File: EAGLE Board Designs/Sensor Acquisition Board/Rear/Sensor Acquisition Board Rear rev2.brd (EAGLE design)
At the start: 92.7 x 50.8 mm, 32 parts, among them J1 JUMPER_0603_, J2 CONNECTOR-4_μF_S_RA_, J3 CONNECTOR-4_μF_S_RA_, J4 CONNECTOR-4_μF_S_RA_, J5 CONNECTOR-4_μF_S_RA_, J6 CONNECTOR-CAN_μF_S_RA_, U1 VOLTAGE_REGULATOR_SOT-223_5V, U2 MCP2562FD

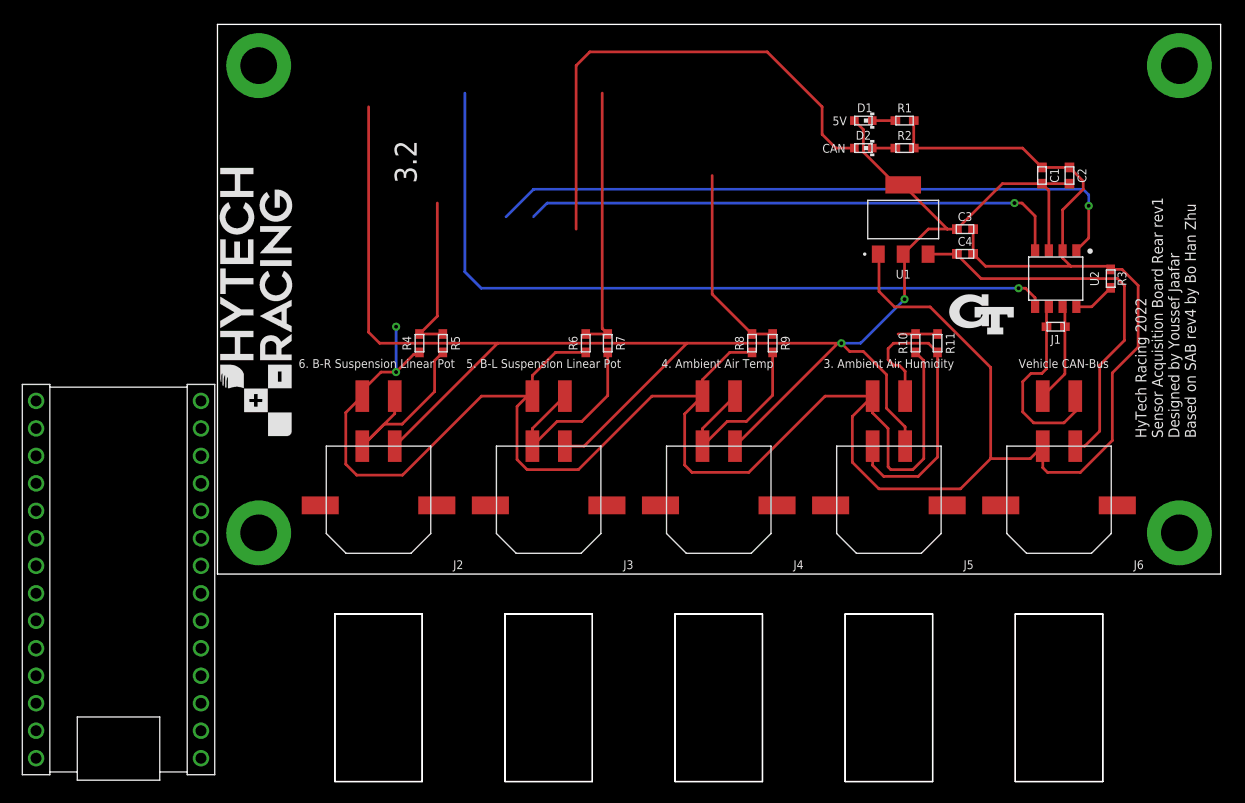
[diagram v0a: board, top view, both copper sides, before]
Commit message: regrounded with groundplane
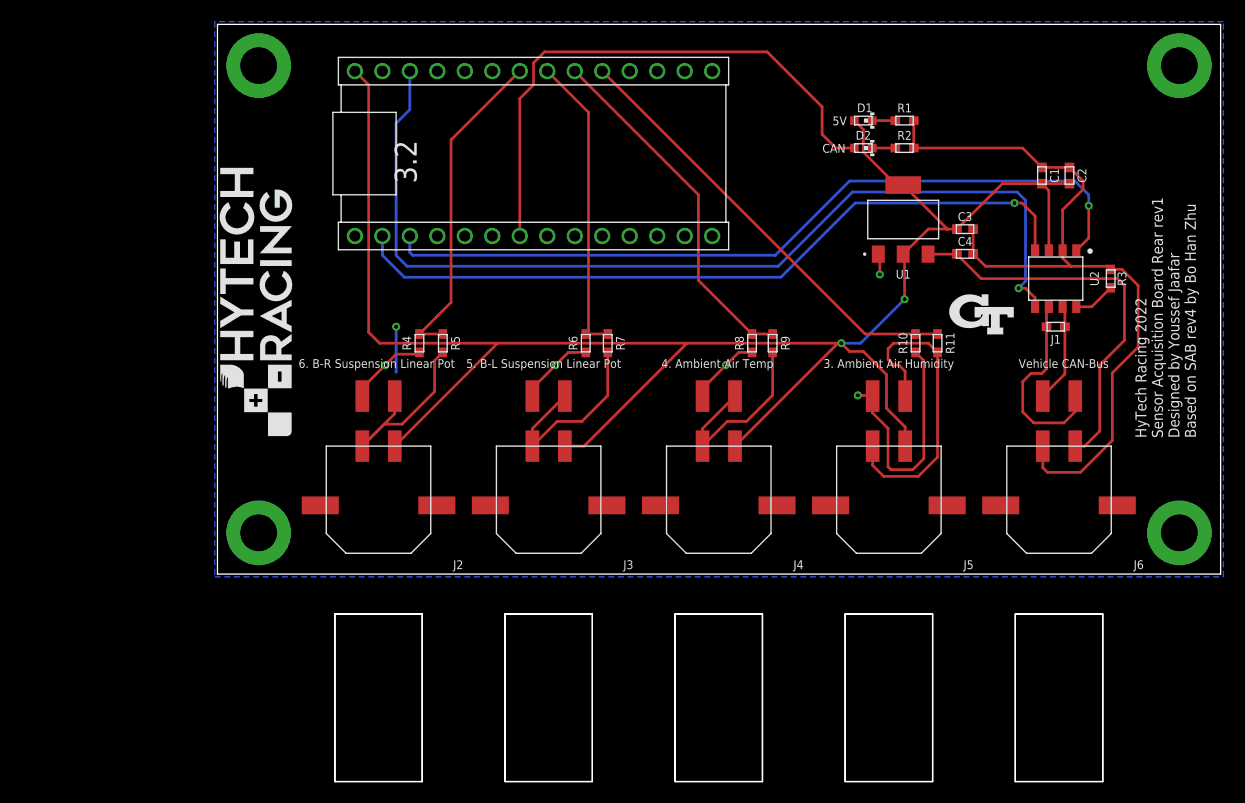
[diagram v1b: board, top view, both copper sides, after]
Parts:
- moved A1 70.0 mm to (12.7, 46.5), turned to 270 degrees
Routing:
- net GND: track 254.4 -> 123.2 mm, vias 2 -> 6
- net SENSOR_3: track 3.64 -> 41.1 mm
- net TEENSY_3.3V: track 71.0 -> 90.4 mm
- net CAN_RX: track 50.6 -> 69.5 mm
- net SENSOR_6: track 14.9 -> 30.3 mm
- net SENSOR_4: track 18.1 -> 33.0 mm
- net CAN_TX: track 60.7 -> 73.4 mm
- net CAN_LED: track 46.5 -> 51.8 mm
- net +5V: track 170.0 -> 173.8 mm
- net SENSOR_5: track 24.5 -> 28.0 mm
- added copper zone on layer 16, net GND

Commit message: Created rear sab board
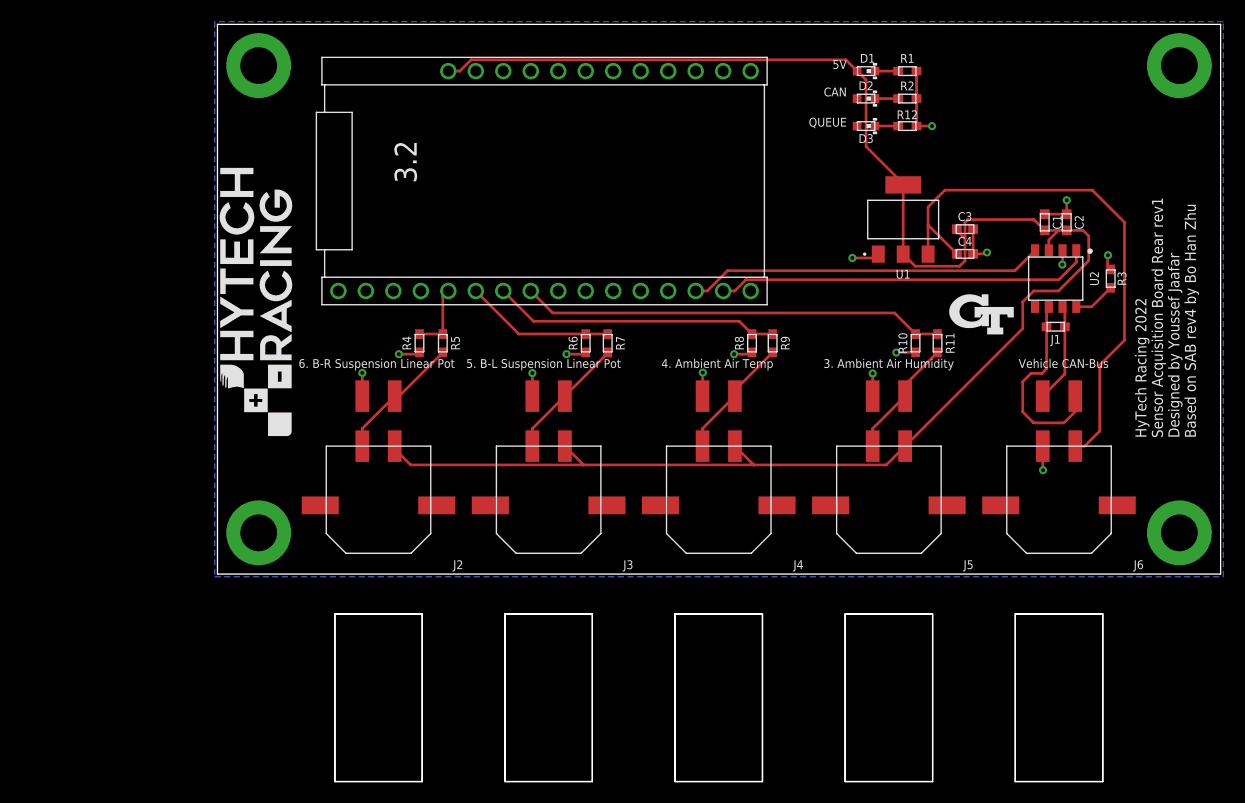
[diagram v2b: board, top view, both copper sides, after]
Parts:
- removed A1: TEENSY_4.0, HyTechDevices:TEENSY_SHORT
- added A2: ESP32, HyTechDevicesTemp:ESP32
- added D3: LED_0603_RED, HyTechDevices:0603-LED
- added R12: RESISTOR_0603_470, HyTechDevices:0603-RES
- moved D1 4.58 mm to (59.9, 46.5)
- moved D2 4.58 mm to (59.9, 43.9)
- moved R1 4.58 mm to (63.8, 46.5)
- moved R2 4.58 mm to (63.8, 43.9)
- moved C1 4.33 mm to (76.5, 32.5)
- moved C2 4.33 mm to (78.5, 32.5)
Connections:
- removed net CAN_RX: A1.D0, U2.4
- removed net CAN_TX: A1.D1, U2.1
- removed net TEENSY_3.3V: A1.3.3V, U2.5
- new net EN: A2.EN
- new net ESP_3.3V: A2.3.3V
- new net N$10: D3.1, R12.1
- new net N$11: A2.D12
- new net N$12: A2.D13
- new net N$13: U2.5
- new net N$4: A2.TX, U2.1
- new net N$8: A2.RX, U2.4
- new net QUEUE_LED: D3.2
- new net RST: A2.RST
- new net USB: A2.USB
- net +5V: now also A2.BAT; no longer A1.VIN
- net CAN_LED: no longer A1.D5
- net GND: now also A2.GND, R12.2; no longer A1.AGND/GND, A1.GND
- net SENSOR_3: now also A2.A3; no longer A1.D17
- net SENSOR_4: now also A2.A2; no longer A1.D18
- net SENSOR_5: now also A2.A1; no longer A1.D19
- net SENSOR_6: now also A2.A0; no longer A1.D20
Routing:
- net TEENSY_3.3V: track 90.4 -> 0.00 mm, vias 1 -> 0
- net GND: track 123.2 -> 37.9 mm, vias 6 -> 15
- net CAN_TX: track 73.4 -> 0.00 mm, vias 1 -> 0
- net CAN_RX: track 69.5 -> 0.00 mm, vias 1 -> 0
- net CAN_LED: track 51.8 -> 0.00 mm
- net N$4: track 0.00 -> 34.8 mm
- net N$8: track 0.00 -> 32.9 mm
- net SENSOR_6: track 30.3 -> 6.35 mm
- net N$9: track 29.1 -> 11.1 mm
- net +12V: track 36.6 -> 51.3 mm
- net SENSOR_5: track 28.0 -> 13.8 mm
- net +5V: track 173.8 -> 164.3 mm, vias 2 -> 0
- net N$7: track 18.8 -> 11.5 mm
- net N$6: track 18.3 -> 11.4 mm
- net N$5: track 18.6 -> 12.0 mm
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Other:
- board text added: "QUEUE"

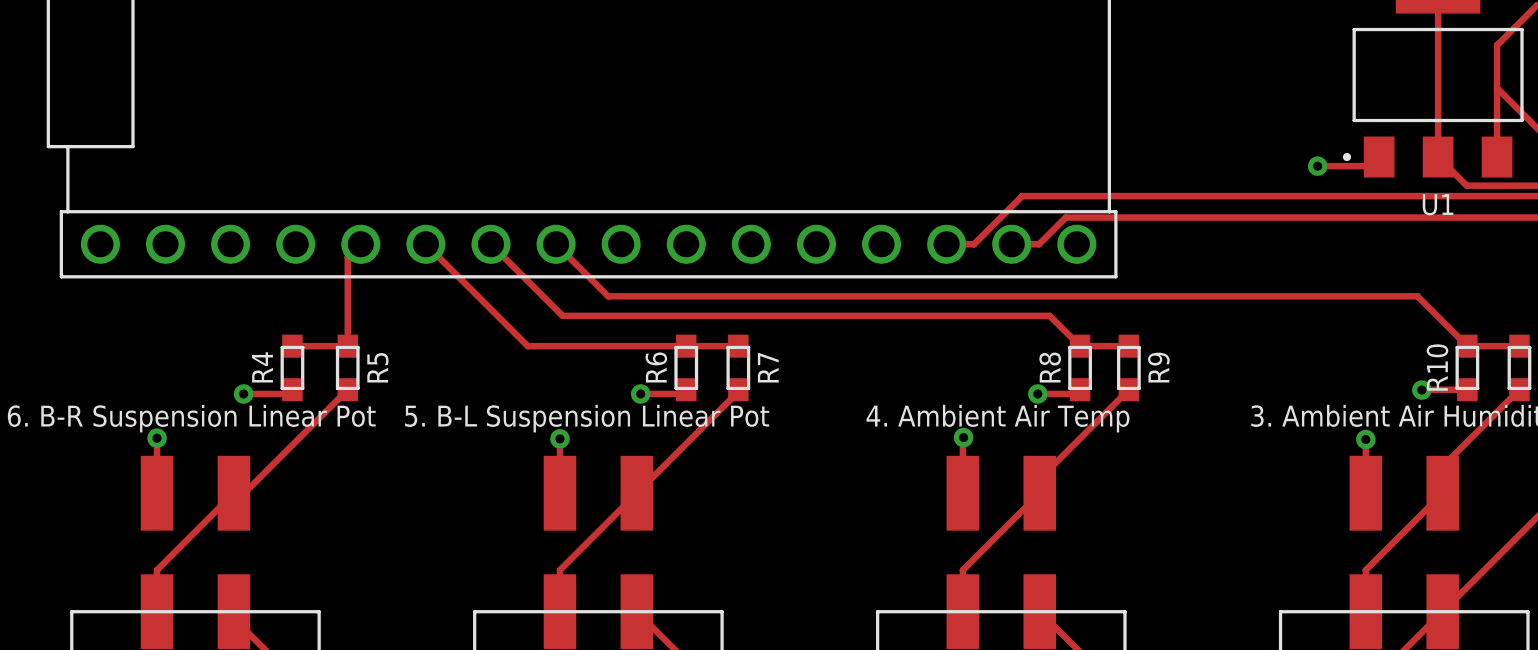
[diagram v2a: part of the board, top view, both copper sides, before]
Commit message: Fixed wire stubs
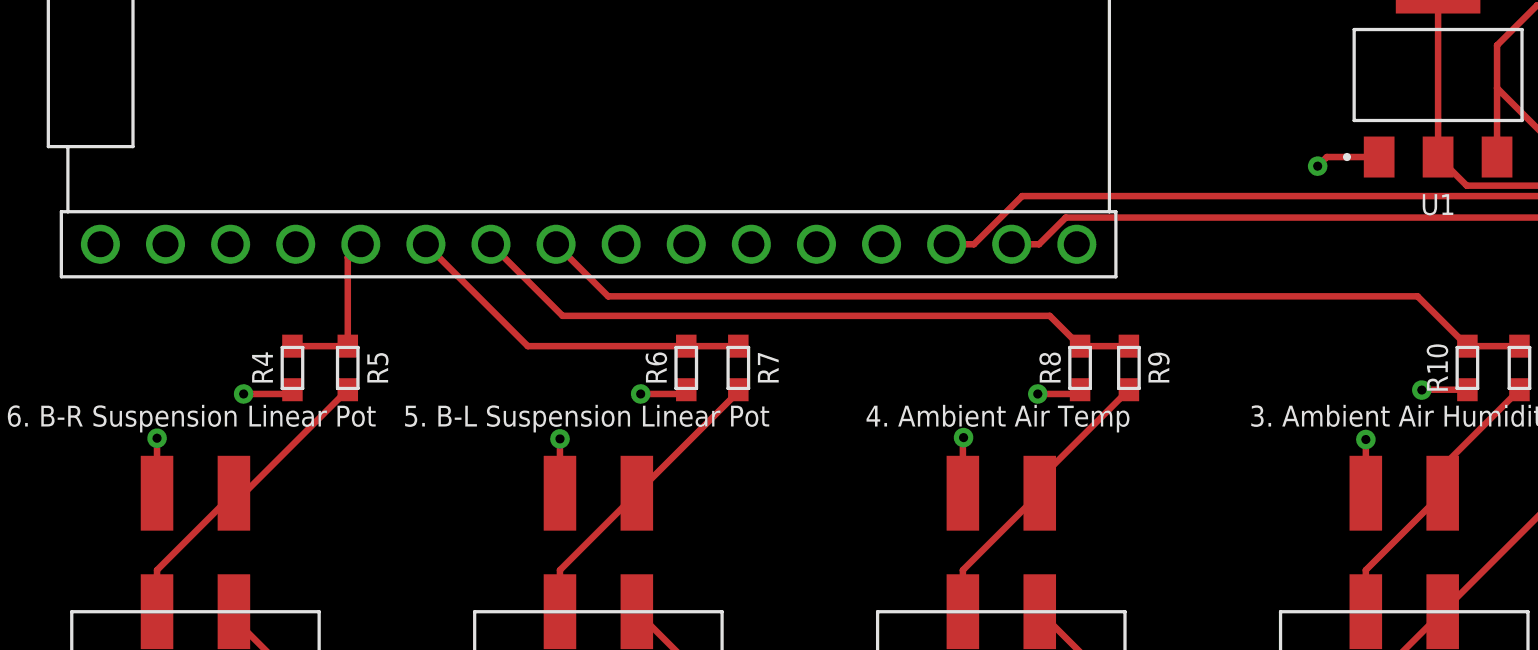
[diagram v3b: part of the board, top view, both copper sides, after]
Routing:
- net GND: track 37.9 -> 36.9 mm
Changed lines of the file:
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@@
 <contactref element="R6" pad="1"/>
 <contactref element="R4" pad="1"/>
-<wire x1="28.6385" y1="16.4465" x2="29.107" y2="16.4465" width="0.254" layer="1"/>
 <wire x1="64.604" y1="46.482" x2="64.604" y2="43.942" width="0.254" layer="1"/>
-<wire x1="61.073" y1="29.566" x2="61.1378" y2="29.5012" width="0.254" layer="1"/>
-<wire x1="13.3844" y1="16.4465" x2="13.3844" y2="16.942325" width="0.254" layer="1"/>
 <contactref element="U2" pad="2"/>
 <contactref element="R3" pad="1"/>
@@
 <wire x1="60.5536" y1="18.542" x2="60.5536" y2="16.4479" width="0.254" layer="1"/>
 <via x="58.674" y="29.21" extent="1-16" drill="0.3556"/>
-<wire x1="61.073" y1="29.566" x2="60.717" y2="29.21" width="0.254" layer="1"/>
-<wire x1="60.717" y1="29.21" x2="58.674" y2="29.21" width="0.254" layer="1"/>
 <contactref element="A2" pad="GND"/>
 <contactref element="R12" pad="2"/>
@@
 <wire x1="18.503" y1="20.32" x2="16.764" y2="20.32" width="0.254" layer="1"/>
 <via x="16.764" y="20.32" extent="1-16" drill="0.3556"/>
-<wire x1="13.3858" y1="18.5928" x2="13.3844" y2="18.5914" width="0.254" layer="1"/>
-<wire x1="13.3844" y1="18.5914" x2="13.3844" y2="16.4465" width="0.254" layer="1"/>
 <via x="13.3858" y="18.5928" extent="1-16" drill="0.3556"/>
 <wire x1="29.107" y1="16.4465" x2="29.1084" y2="16.4479" width="0.254" layer="1"/>
-<wire x1="29.1084" y1="16.4479" x2="29.1084" y2="18.5674" width="0.254" layer="1"/>
 <via x="29.1084" y="18.5674" extent="1-16" drill="0.3556"/>
 <wire x1="44.8296" y1="16.4465" x2="44.8296" y2="18.5914" width="0.254" layer="1"/>
@@
 <wire x1="64.604" y1="41.402" x2="66.04" y2="41.402" width="0.254" layer="1"/>
 <via x="66.04" y="41.402" extent="1-16" drill="0.3556"/>
+<wire x1="29.107" y1="16.4465" x2="29.107" y2="18.566" width="0.254" layer="1"/>
+<wire x1="29.107" y1="18.566" x2="29.1084" y2="18.5674" width="0.254" layer="1"/>
+<wire x1="58.674" y1="29.21" x2="59.03" y2="29.566" width="0.254" layer="1"/>
+<wire x1="59.03" y1="29.566" x2="61.073" y2="29.566" width="0.254" layer="1"/>
+<wire x1="13.3844" y1="16.4465" x2="13.3844" y2="18.5914" width="0.254" layer="1"/>
+<wire x1="13.3844" y1="18.5914" x2="13.3858" y2="18.5928" width="0.254" layer="1"/>
 </signal>
 <signal name="+5V">

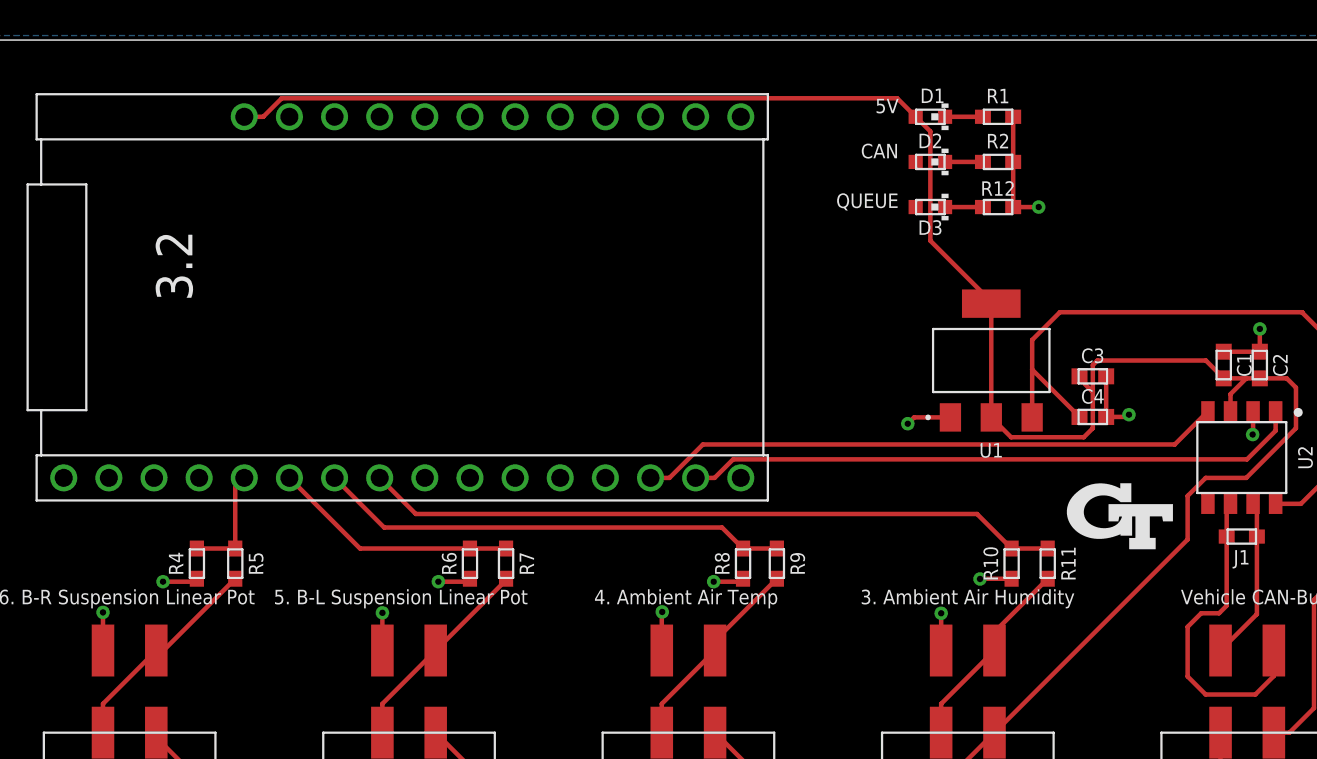
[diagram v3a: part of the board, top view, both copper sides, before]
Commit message: Fixed labeling and incorrect connections
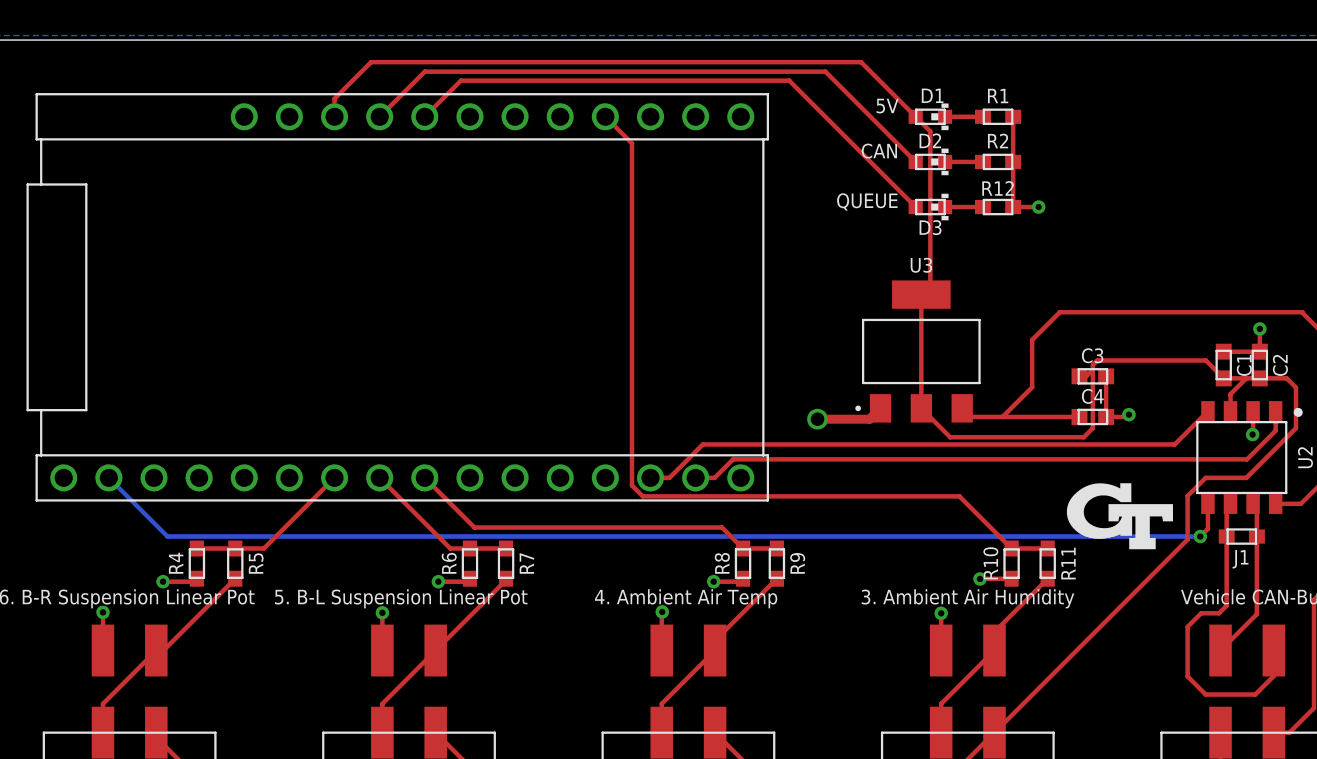
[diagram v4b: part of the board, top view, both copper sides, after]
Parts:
- removed U1: VOLTAGE_REGULATOR_SOT-223_5V, HyTechDevices:SOT-223
- added U3: VOLTAGE_REGULATOR_SOT-223_5V, HyTechDevices:SOT-223
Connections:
- removed net N$11: A2.D12
- removed net N$12: A2.D13
- removed net N$13: U2.5
- removed net SENSOR_3: A2.A3, R10.2, R11.1
- removed net SENSOR_4: A2.A2, R8.2, R9.1
- removed net SENSOR_5: A2.A1, R6.2, R7.1
- removed net SENSOR_6: A2.A0, R4.2, R5.1
- removed net USB: A2.USB
- new net AMB_HUM: A2.D32, R10.2, R11.1
- new net AMB_TEMP: A2.A4, R8.2, R9.1
- new net BAT: A2.BAT
- new net SUSP_BL: A2.A3, R6.2, R7.1
- new net SUSP_BR: A2.A2, R4.2, R5.1
- net +12V: now also U3.3; no longer U1.3
- net +5V: now also A2.USB, U3.2, U3.4; no longer A2.BAT, U1.2, U1.4
- net CAN_LED: now also A2.D13
- net ESP_3.3V: now also U2.5
- net GND: now also U3.1; no longer U1.1
- net QUEUE_LED: now also A2.D12
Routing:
- net ESP_3.3V: track 0.00 -> 64.8 mm, vias 0 -> 1
- net AMB_HUM: track 0.00 -> 46.2 mm
- net SENSOR_3: track 39.2 -> 0.00 mm
- net CAN_LED: track 0.00 -> 33.3 mm
- net QUEUE_LED: track 0.00 -> 31.4 mm
- net SENSOR_4: track 26.5 -> 0.00 mm
- net AMB_TEMP: track 0.00 -> 21.5 mm
- net SENSOR_5: track 13.8 -> 0.00 mm
- net SUSP_BR: track 0.00 -> 9.39 mm
- net SUSP_BL: track 0.00 -> 8.76 mm
- net SENSOR_6: track 6.35 -> 0.00 mm
- net +12V: track 51.3 -> 55.0 mm
- net GND: track 36.9 -> 38.1 mm
- net +5V: track 164.3 -> 163.7 mm
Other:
- board text removed: "3.2"
